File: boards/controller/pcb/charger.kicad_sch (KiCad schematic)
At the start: 29 parts, among them J401 Battery, U401 BQ25792RQMR

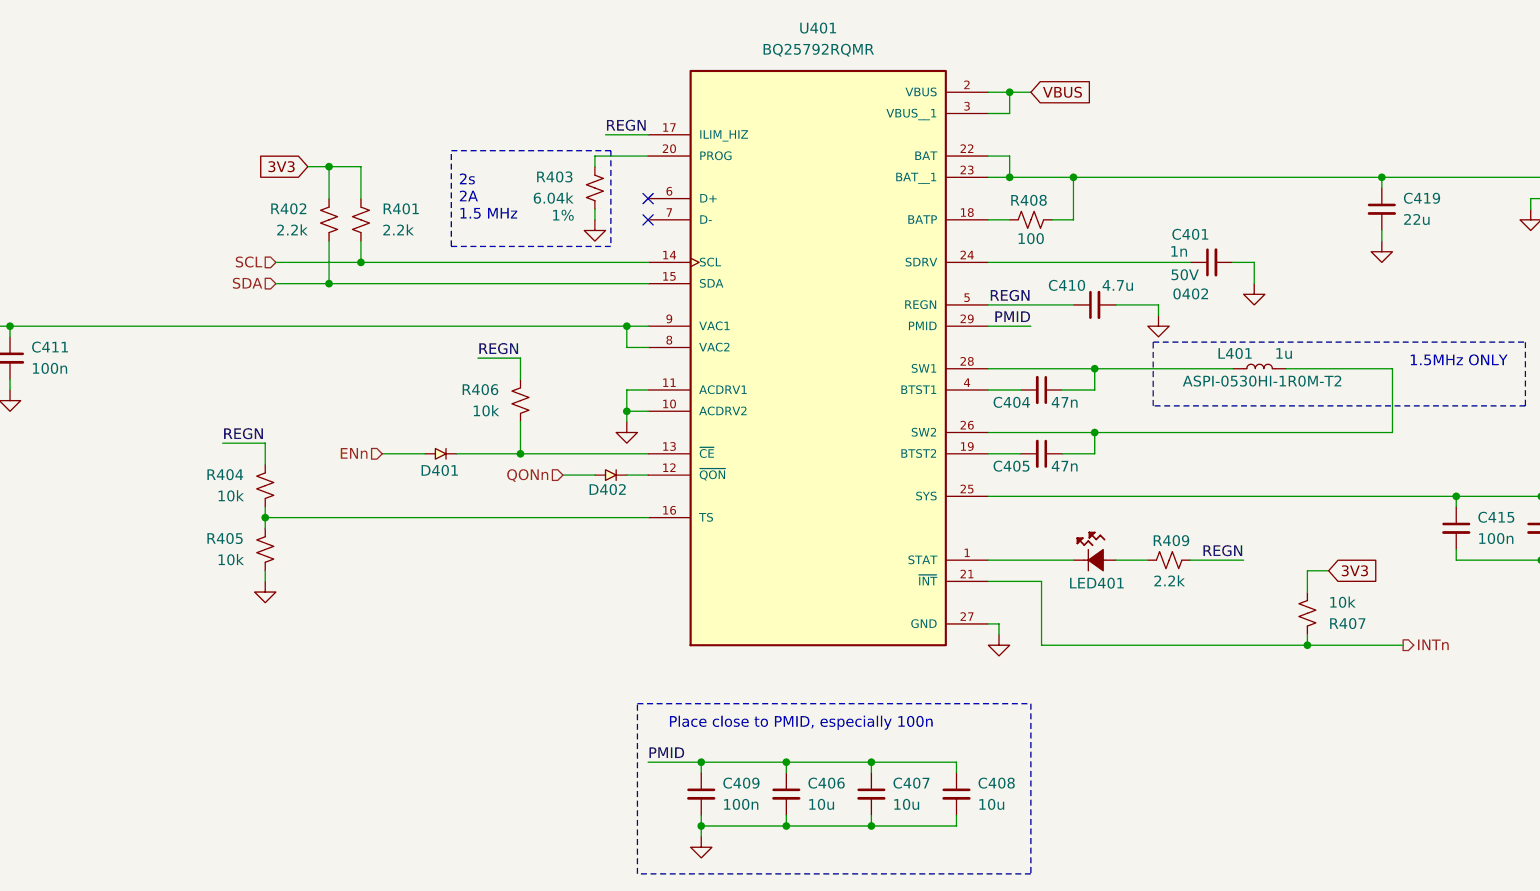
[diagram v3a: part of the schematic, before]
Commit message: controller: pcb: Update schematic
Signed-off-by: Nicholas Loehrke <nicholasnloehrke@gmail.com>
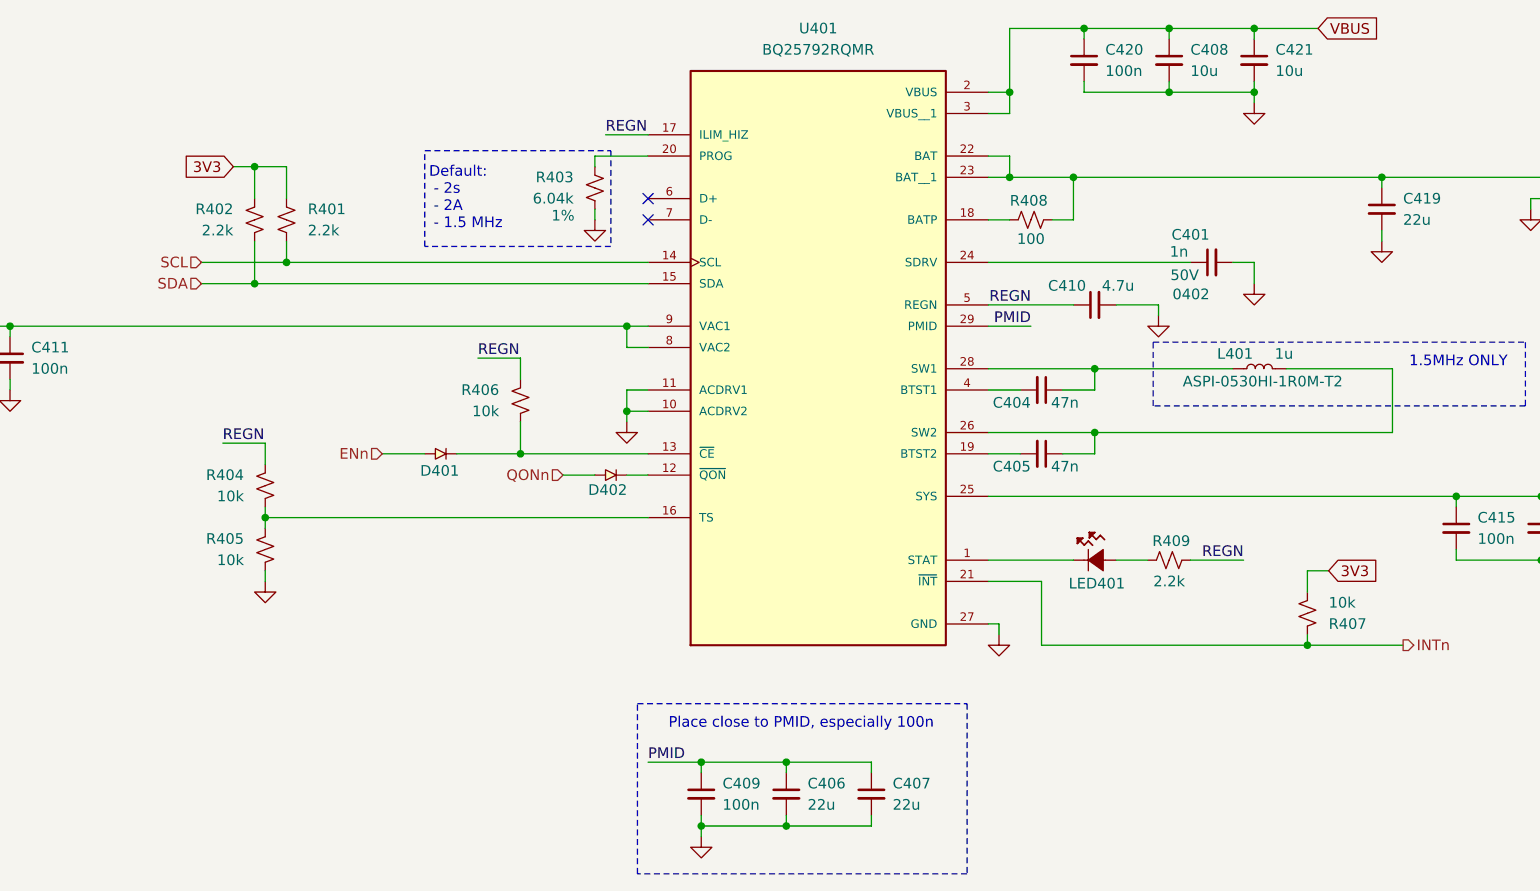
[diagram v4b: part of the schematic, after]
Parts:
- added C420: 100n, symbol Device:C_Small
- added C421: 10u, symbol Device:C_Small
- C406, C407: value 10u -> 22u
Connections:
- net GND: now also C420.2, C421.2
- net PMID: no longer C408.1
- net VBUS: now also C408.1, C420.1, C421.1
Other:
- note added: "Default: - 2s - 2A - 1.5 MHz"
- note removed: "2s 2A 1.5 MHz"
- moved on the sheet: R401, R402

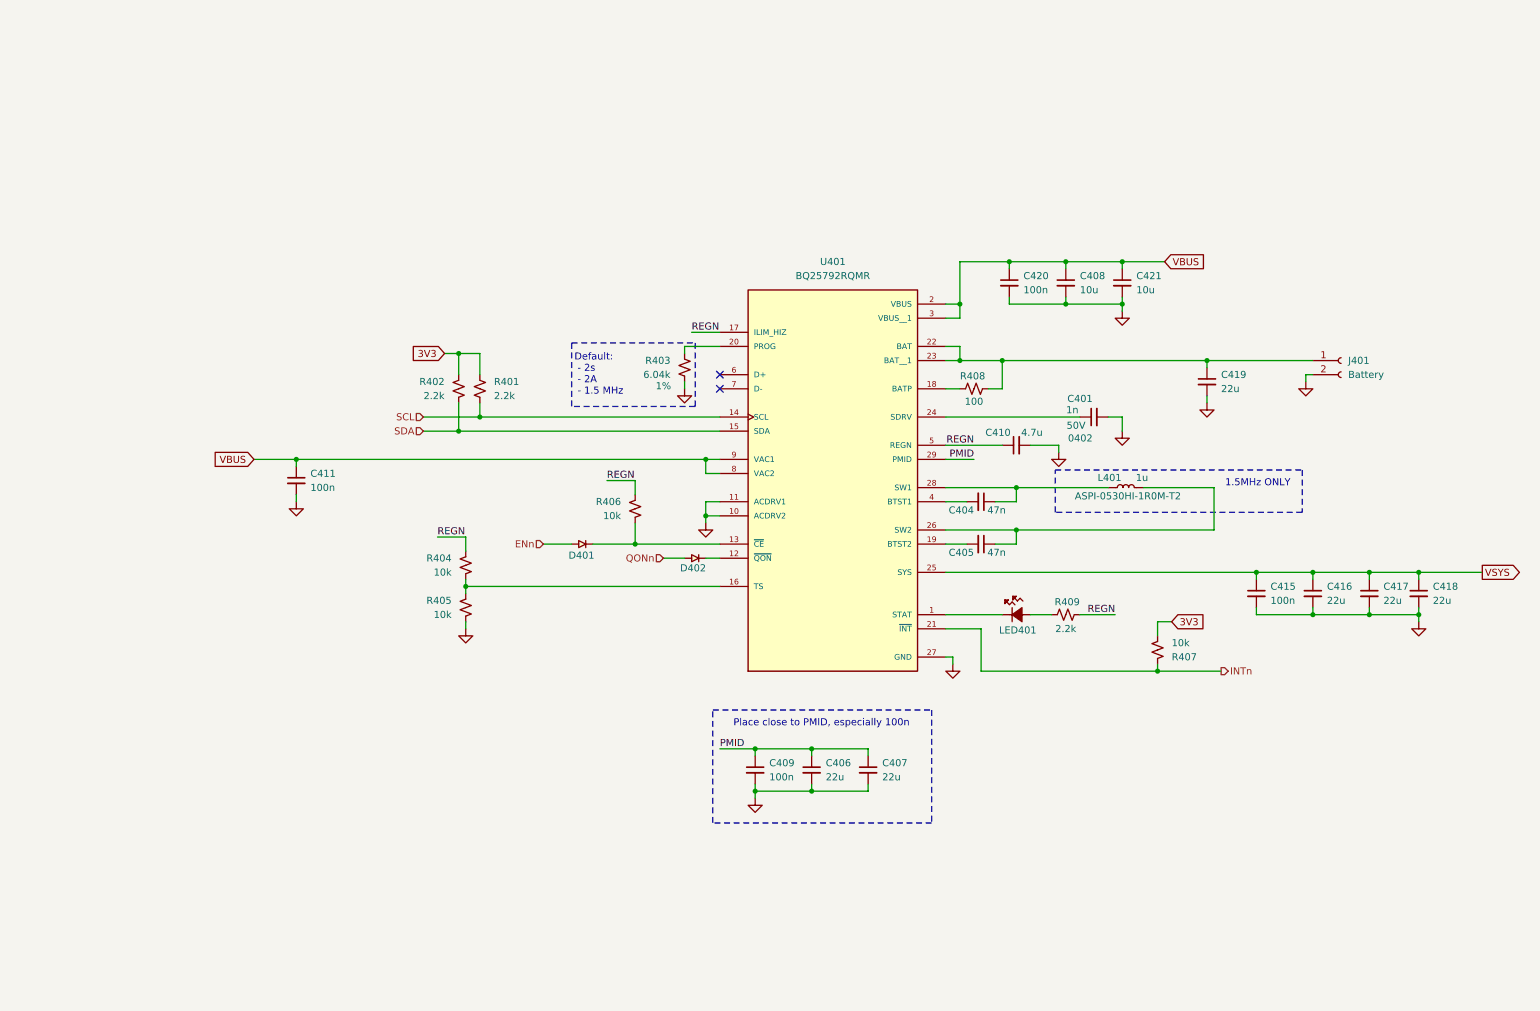
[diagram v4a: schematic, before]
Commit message: controller: pcb: Update schematic
Signed-off-by: Nicholas Loehrke <nicholasnloehrke@gmail.com>
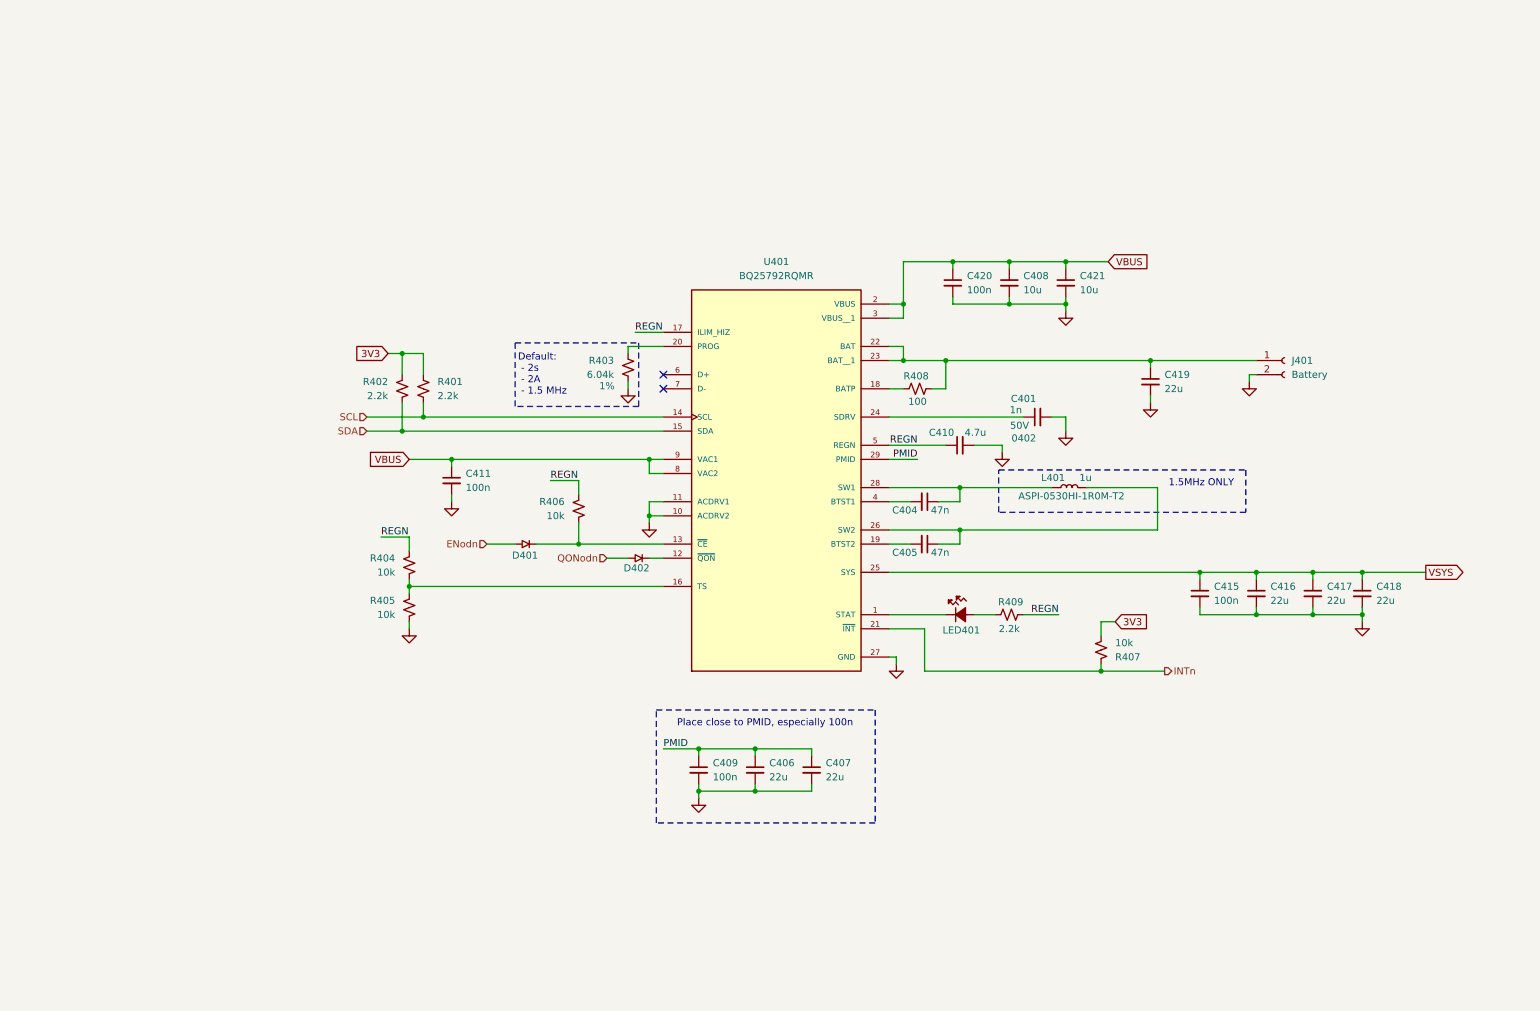
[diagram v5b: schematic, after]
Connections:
- net ENn renamed ENodn
- net QONn renamed QONodn
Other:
- moved on the sheet: C401, C404, C405, C406, C407, C408, C409, C410, C411, C415, C416, C417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

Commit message: controller: pcb: Update schematic
Signed-off-by: Nicholas Loehrke <nicholasnloehrke@gmail.com>
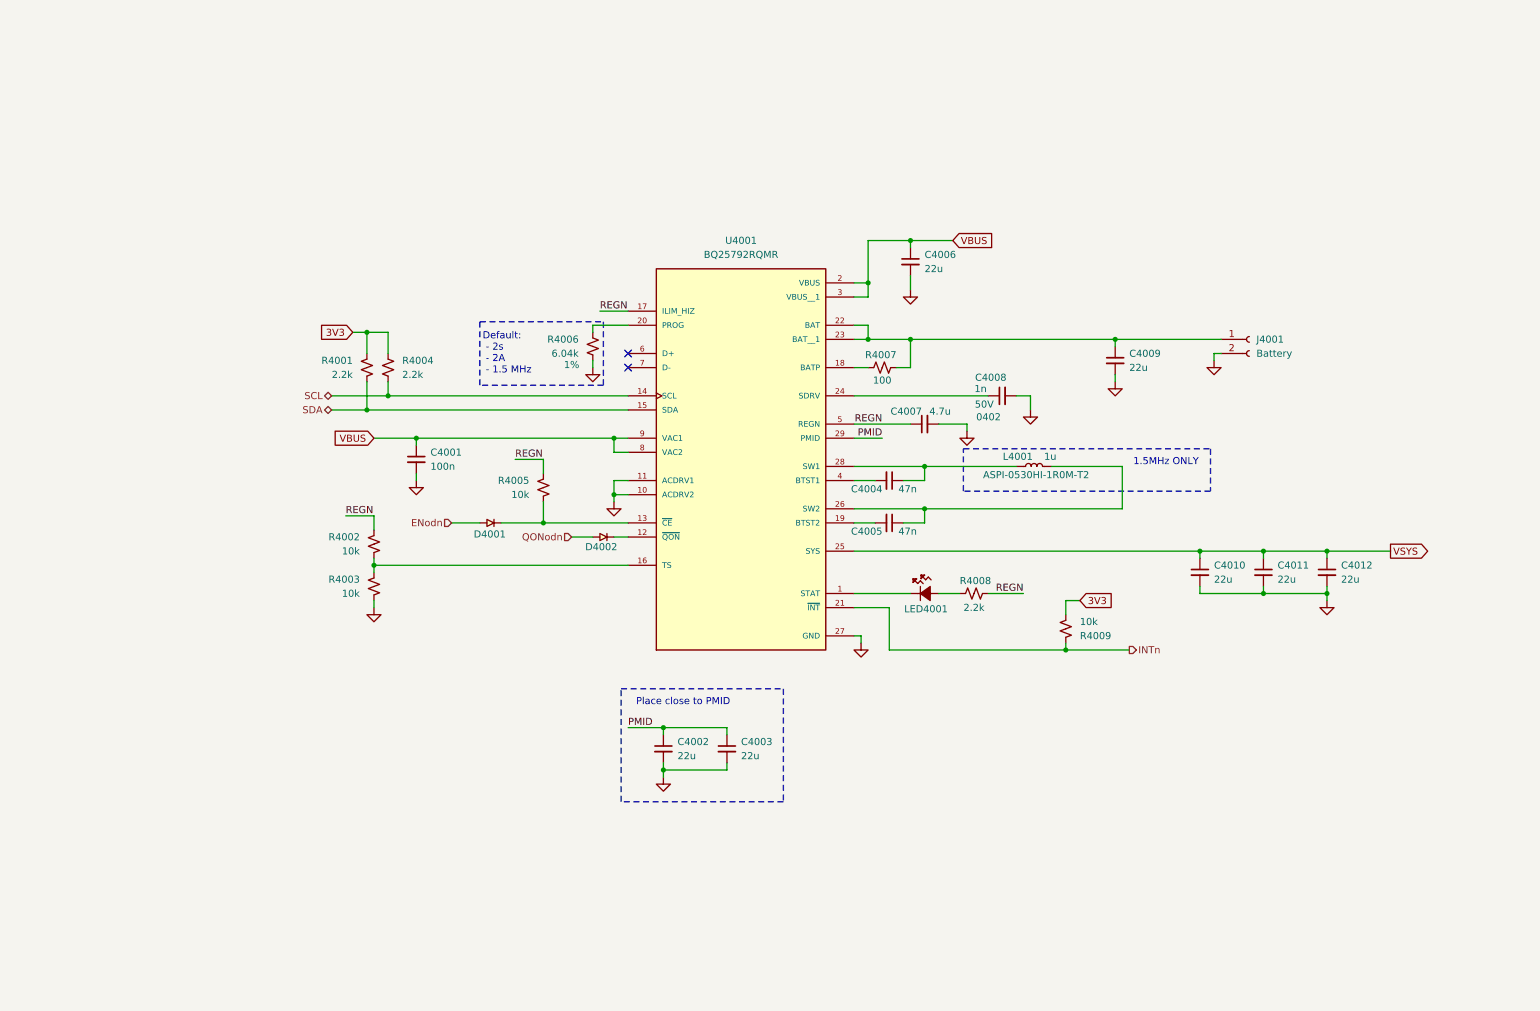
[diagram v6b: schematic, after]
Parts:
- removed C407: 22u, symbol Device:C_Small
- removed C408: 10u, symbol Device:C_Small
- removed C415, C420: 100n, symbol Device:C_Small
- C4002: renamed from C409; value 100n -> 22u
- C4006: renamed from C421; value 10u -> 22u
- renumbered C411 to C4001, C406 to C4003, C404 to C4004, C405 to C4005, C410 to C4007, C401 to C4008, C419 to C4009, C416 to C4010, C417 to C4011, C418 to C4012, D401 to D4001, D402 to D4002, J401 to J4001, L401 to L4001, LED401 to LED4001, R402 to R4001, R404 to R4002, R405 to R4003, R401 to R4004, R406 to R4005, R403 to R4006, R408 to R4007, R409 to R4008, R407 to R4009, U401 to U4001
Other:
- note added: "Place close to PMID"
- note removed: "Place close to PMID, especially 100n"
- moved on the sheet: C4001, C4002, C4003, C4004, C4005, C4006, C4007, C4008, C4009, C4010, C4011, C4012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

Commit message: controller: pcb: Update schematic
- Replace 22u caps with 10u since 22u are very expensive
- Add TCC and MPN fields

Signed-off-by: Nicholas Loehrke <nicholasnloehrke@gmail.com>
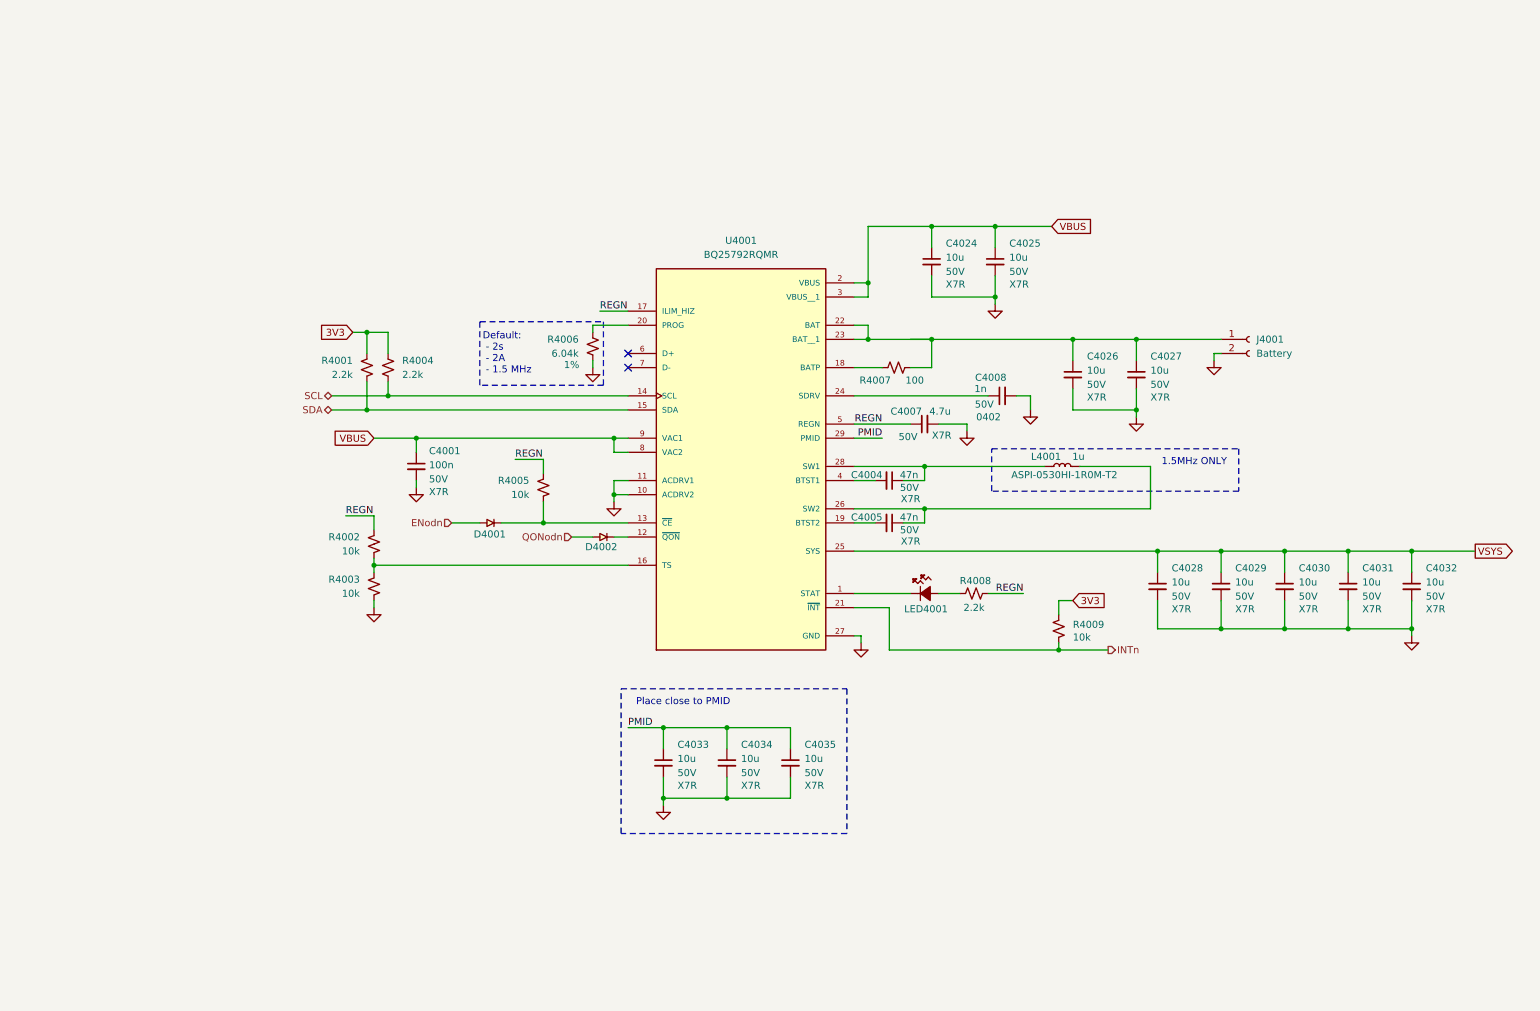
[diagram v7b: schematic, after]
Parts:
- removed C4002, C4003, C4006, C4009, C4010, C4011, C4012: 22u, symbol Device:C_Small
- added C4024, C4025, C4026, C4027, C4028, C4029, C4030, C4031, C4032, C4033, C4034, C4035: 10u, symbol Device:C_Small
- C4001, C4004, C4005, C4007: TCC (none) -> X7R; Voltage (none) -> 50V
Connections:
- net GND: now also C4024.2, C4025.2, C4026.2, C4027.2, C4028.2, C4029.2, C4030.2, C4031.2, C4032.2, C4033.2, C4034.2, C4035.2
- net PMID: now also C4033.1, C4034.1, C4035.1
- net VBUS: now also C4024.1, C4025.1
- net VSYS: now also C4028.1, C4029.1, C4030.1, C4031.1, C4032.1
- net at J4001.1 (Pin_1), R4007.2, U4001.22 (BAT)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: now also C4026.1, C4027.1
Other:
- moved on the sheet: C4001, L4001, R4007, R4009
